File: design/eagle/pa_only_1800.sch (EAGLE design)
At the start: 53 parts, among them J1 DC_IN, J2 5V_OUT, U1 RF3865, U2 ALM32220, U3 MIC29301-5.0BT

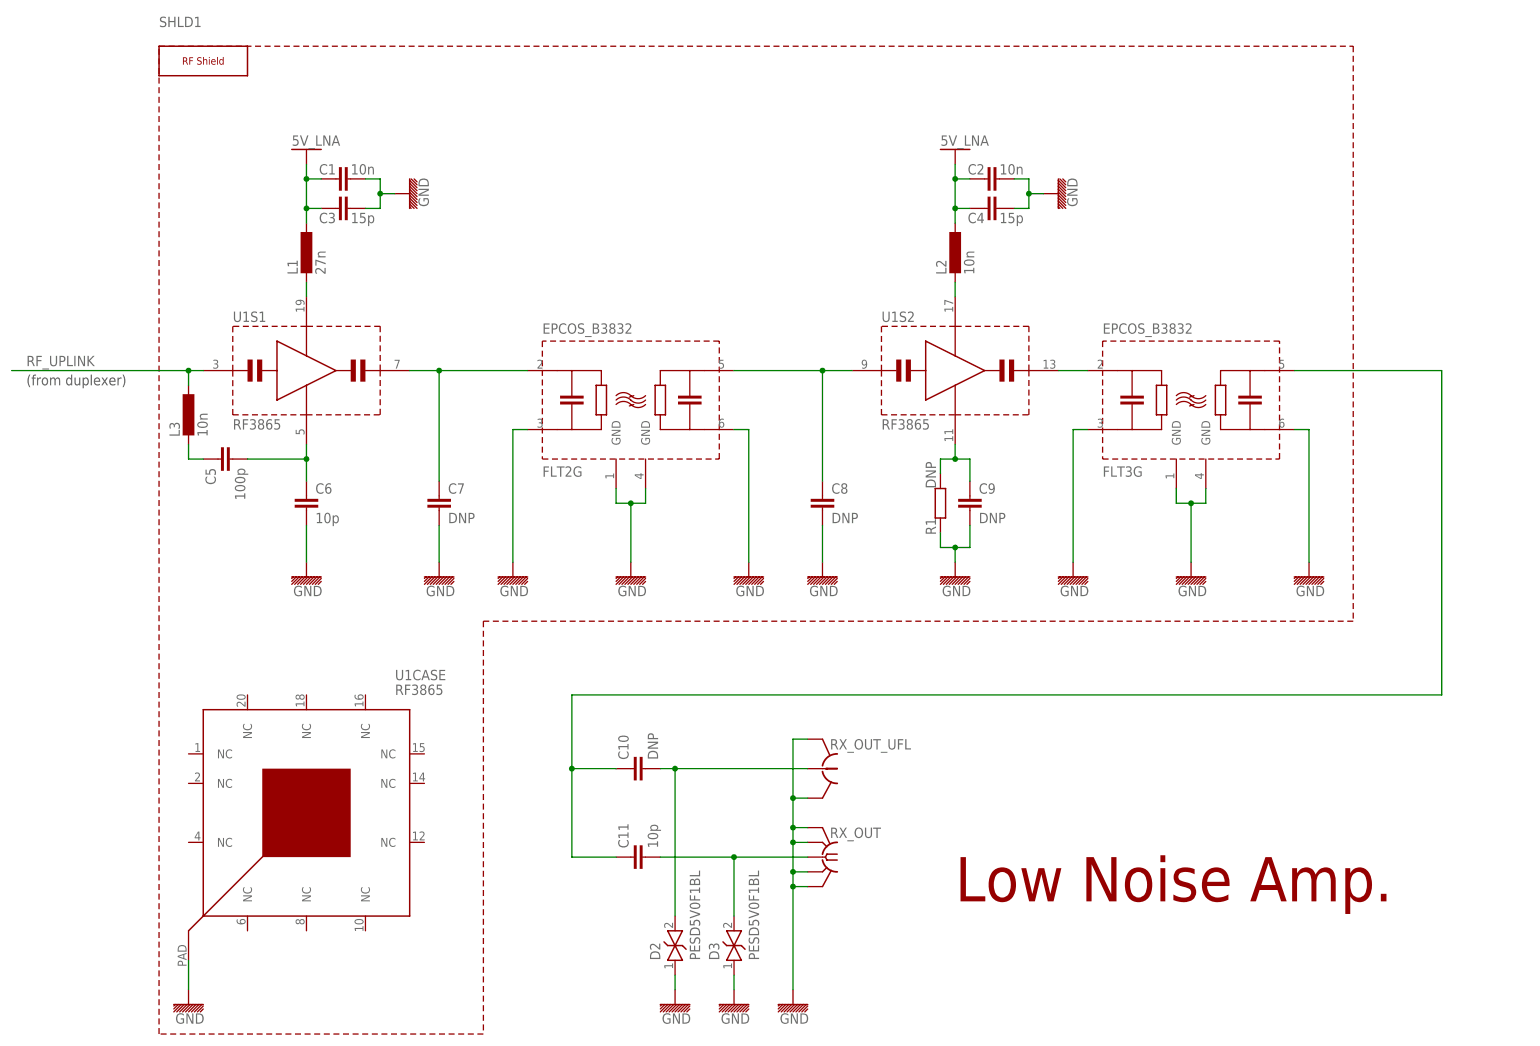
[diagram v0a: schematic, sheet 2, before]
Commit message: add a PA-only version without LNA for DCS 1800
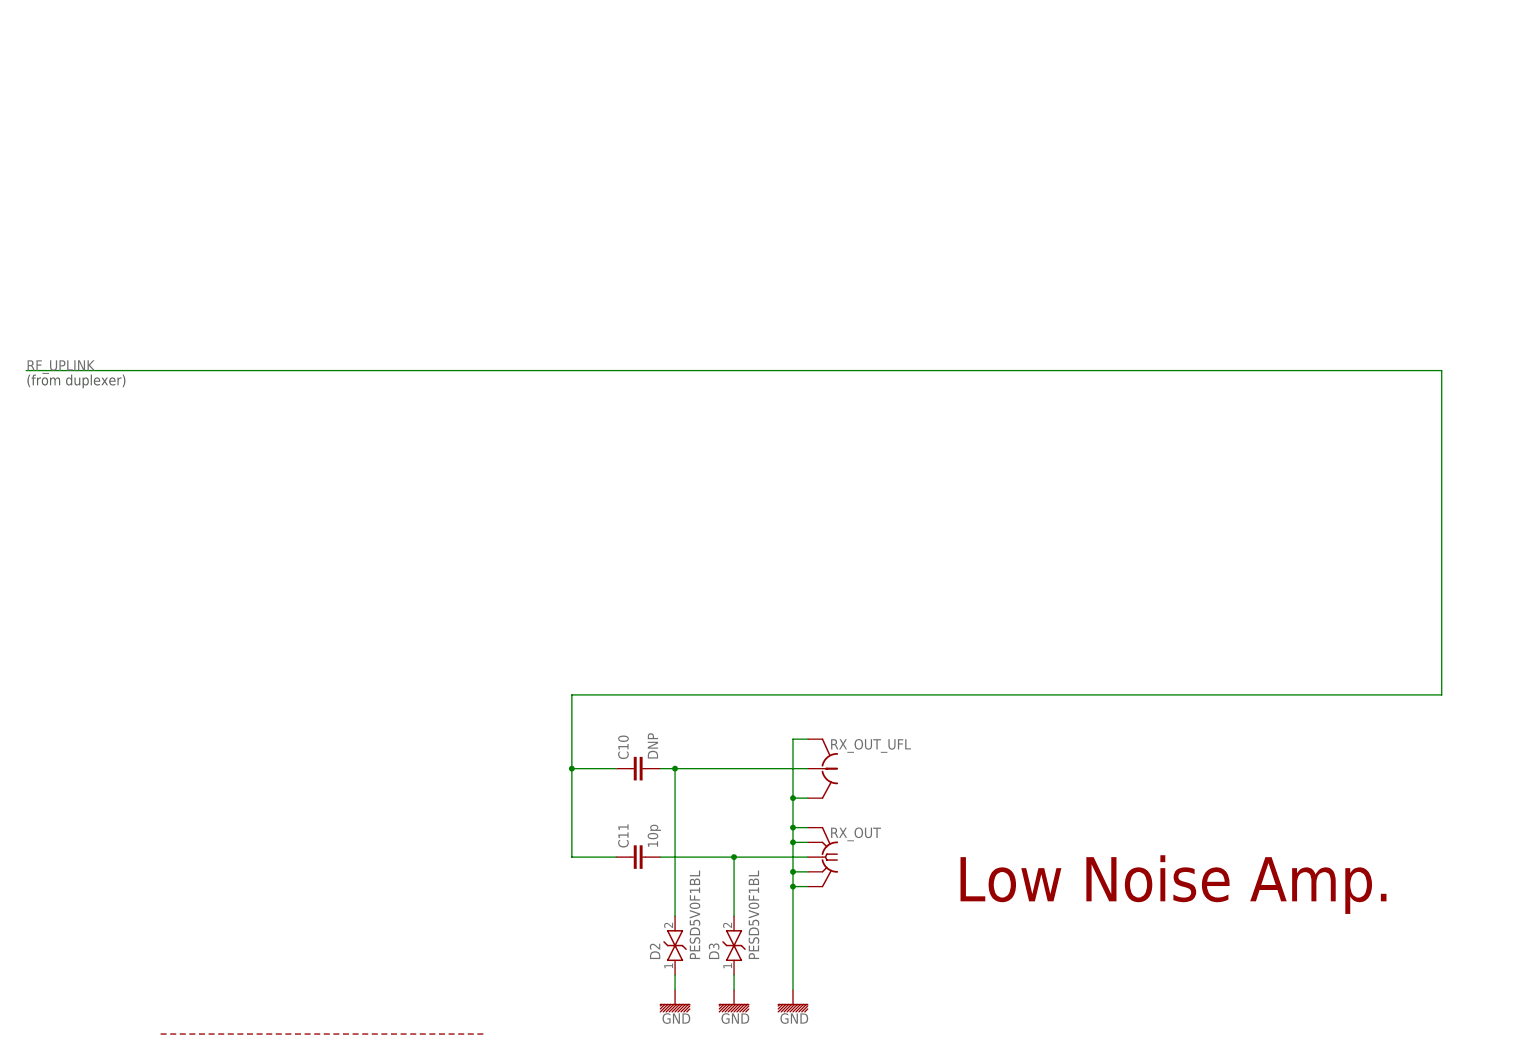
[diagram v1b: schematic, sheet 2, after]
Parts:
- removed C1, C2: 10n, we_passive:C-EU_0603
- removed C26: 10u, rcl:CPOL-EUSMCA
- removed C3, C4: 15p, we_passive:C-EU_0603
- removed C5: 100p, we_passive:C-EU_0603
- removed C6: 10p, we_passive:C-EU_0603
- removed C7, C8, C9: DNP, we_passive:C-EU_0603
- removed FB4: (no value), we_passive:FBEAD_0603
- removed FLT2, FLT3: EPCOS_B3832, we_passive:EPCOS_B3832
- removed L1: 27n, we_passive:L-EU_0603
- removed L2, L3: 10n, we_passive:L-EU_0603
- removed R1: DNP, we_passive:R-EU_0603
- removed SHLD1: (no value), we_mech:SHIELD25X25
- removed U1: RF3865, we_chips:RF3865
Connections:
- removed net 5V_LNA: C1.1, C2.1, C26.+, C3.1, C4.1, FB4.2, L1.1, L2.1
- removed net N$1: L1.2, U1S1.VDD
- removed net N$10: L2.2, U1S2.VDD
- removed net N$4: C5.1, L3.2
- removed net N$5: C5.2, C6.1, U1S1.AC_GND
- removed net N$6: C9.1, R1.2, U1S2.AC_GND
- removed net N$9: C10.1, C11.1, FLT3G.OUT
- removed net RF_UPLINK_IS_IN: C8.1, FLT2G.OUT, U1S2.RF_IN
- removed net RF_UPLINK_IS_OUT: C7.1, FLT2G.IN, U1S1.RF_OUT
- removed net RF_UPLINK_LNA_OUT: FLT3G.IN, U1S2.RF_OUT
- net 5V: no longer FB4.1
- net GND: no longer C1.2, C2.2, C26.-, C3.2, C4.2, C6.2, C7.2, C8.2, C9.2, FLT2CASE.GND@1, FLT2CASE.GND@2, FLT2G.IN_GND, FLT2G.OUT_GND, FLT3CASE.GND@1, FLT3CASE.GND@2, FLT3G.IN_GND, FLT3G.OUT_GND, R1.1, U1CASE.CASE_GND
- net RF_UPLINK: now also C10.1, C11.1; no longer L3.1, U1S1.RF_IN
